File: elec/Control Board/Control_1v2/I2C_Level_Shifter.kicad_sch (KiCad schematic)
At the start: 21 parts, among them J201 0.100_2Pin, J202 Conn_01x04, Q201 BSS138, Q202 BSS138

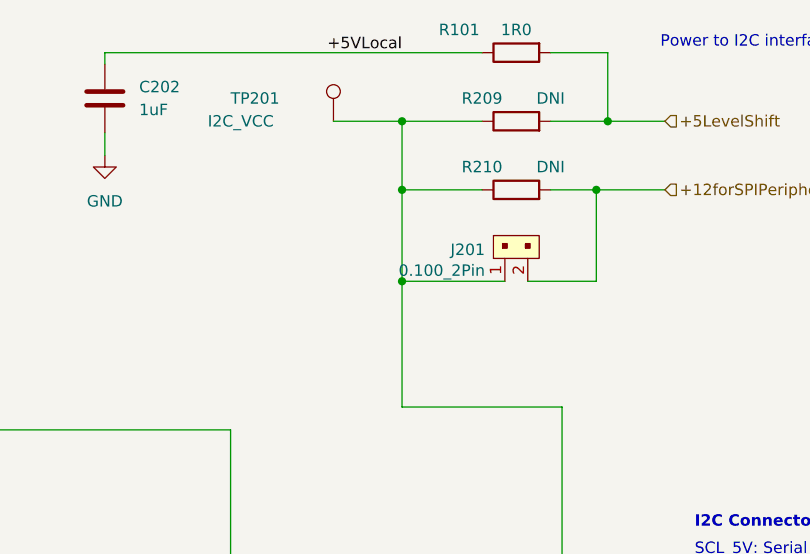
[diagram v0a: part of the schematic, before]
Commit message: PCB V1.2. Add test points of many colors.
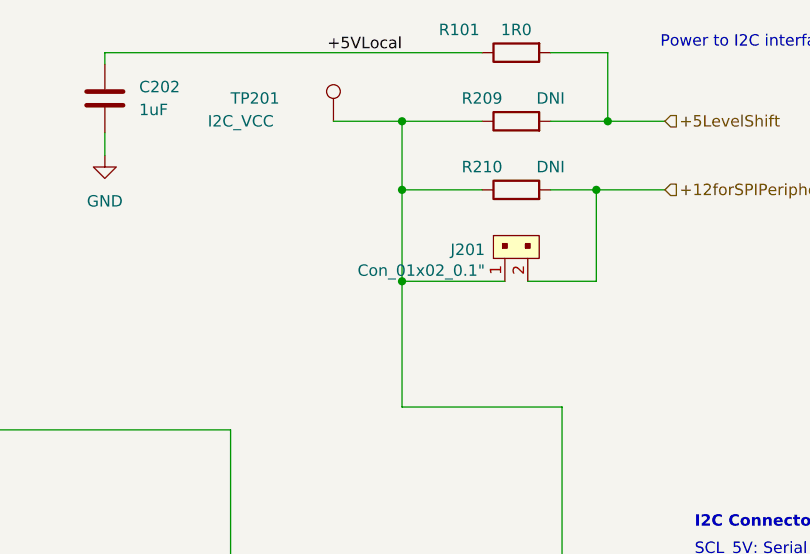
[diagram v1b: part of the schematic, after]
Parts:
- J201: value 0.100_2Pin -> Con_01x02_0.1"; Cost 0.1458 -> 0.0115; Distributor 1 PN C168673 -> C492401; MPN 68000-102HLF -> PZ254V-11-02P; Manufacturer Amphenol ICC -> XFCN
- TP201, TP202, TP203: Cost NA -> 0.0696; Distributor 1 NA -> JLCPCB; Distributor 1 PN NA -> C5277086; MPN (none) -> RH-5000; Manufacturer (none) -> ronghe
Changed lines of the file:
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@@
       (effects (font (size 1.27 1.27)) hide)
     )
-    (property "Distributor 1" "NA" (at 251.46 140.97 0)
-      (effects (font (size 1.27 1.27)) hide)
-    )
-    (property "Distributor 1 PN" "NA" (at 251.46 140.97 0)
-      (effects (font (size 1.27 1.27)) hide)
-    )
-    (property "Cost" "NA" (at 251.46 140.97 0)
+    (property "Distributor 1" "JLCPCB" (at 251.46 140.97 0)
+      (effects (font (size 1.27 1.27)) hide)
+    )
+    (property "Distributor 1 PN" "C5277086" (at 251.46 140.97 0)
+      (effects (font (size 1.27 1.27)) hide)
+    )
+    (property "Cost" "0.0696" (at 251.46 140.97 0)
       (effects (font (size 1.27 1.27)) hide)
     )
     (property "LongLead" "NO" (at 251.46 140.97 0)
+      (effects (font (size 1.27 1.27)) hide)
+    )
+    (property "Description" "Test Points/Test Rings ROHS red" (at 251.46 140.97 0)
+      (effects (font (size 1.27 1.27)) hide)
+    )
+    (property "MPN" "RH-5000 " (at 251.46 140.97 0)
+      (effects (font (size 1.27 1.27)) hide)
+    )
+    (property "Manufacturer" "ronghe " (at 251.46 140.97 0)
       (effects (font (size 1.27 1.27)) hide)
     )
@@
       (effects (font (size 1.27 1.27)) hide)
     )
-    (property "Distributor 1" "NA" (at 251.46 125.73 0)
-      (effects (font (size 1.27 1.27)) hide)
-    )
-    (property "Distributor 1 PN" "NA" (at 251.46 125.73 0)
-      (effects (font (size 1.27 1.27)) hide)
-    )
-    (property "Cost" "NA" (at 251.46 125.73 0)
+    (property "Distributor 1" "JLCPCB" (at 251.46 125.73 0)
+      (effects (font (size 1.27 1.27)) hide)
+    )
+    (property "Distributor 1 PN" "C5277086" (at 251.46 125.73 0)
+      (effects (font (size 1.27 1.27)) hide)
+    )
+    (property "Cost" "0.0696" (at 251.46 125.73 0)
       (effects (font (size 1.27 1.27)) hide)
     )
     (property "LongLead" "NO" (at 251.46 125.73 0)
+      (effects (font (size 1.27 1.27)) hide)
+    )
+    (property "Description" "Test Points/Test Rings ROHS red" (at 251.46 125.73 0)
+      (effects (font (size 1.27 1.27)) hide)
+    )
+    (property "MPN" "RH-5000 " (at 251.46 125.73 0)
+      (effects (font (size 1.27 1.27)) hide)
+    )
+    (property "Manufacturer" "ronghe " (at 251.46 125.73 0)
       (effects (font (size 1.27 1.27)) hide)
     )
@@
       (effects (font (size 1.27 1.27)) hide)
     )
-    (property "Distributor 1" "NA" (at 238.76 68.58 0)
-      (effects (font (size 1.27 1.27)) hide)
-    )
-    (property "Distributor 1 PN" "NA" (at 238.76 68.58 0)
-      (effects (font (size 1.27 1.27)) hide)
-    )
-    (property "Cost" "NA" (at 238.76 68.58 0)
+    (property "Distributor 1" "JLCPCB" (at 238.76 68.58 0)
+      (effects (font (size 1.27 1.27)) hide)
+    )
+    (property "Distributor 1 PN" "C5277086" (at 238.76 68.58 0)
+      (effects (font (size 1.27 1.27)) hide)
+    )
+    (property "Cost" "0.0696" (at 238.76 68.58 0)
       (effects (font (size 1.27 1.27)) hide)
     )
     (property "LongLead" "NO" (at 238.76 68.58 0)
+      (effects (font (size 1.27 1.27)) hide)
+    )
+    (property "Description" "Test Points/Test Rings ROHS red" (at 238.76 68.58 0)
+      (effects (font (size 1.27 1.27)) hide)
+    )
+    (property "MPN" "RH-5000 " (at 238.76 68.58 0)
+      (effects (font (size 1.27 1.27)) hide)
+    )
+    (property "Manufacturer" "ronghe " (at 238.76 68.58 0)
       (effects (font (size 1.27 1.27)) hide)
     )
@@
       (effects (font (size 1.27 1.27)) (justify right))
     )
-    (property "Value" "0.100_2Pin" (at 255.6002 85.1662 0)
+    (property "Value" "Con_01x02_0.1\"" (at 255.6002 85.1662 0)
       (effects (font (size 1.27 1.27)) (justify right))
     )
@@
       (effects (font (size 1.524 1.524)) (justify left) hide)
     )
-    (property "MPN" "68000-102HLF" (at 262.89 96.52 0)
+    (property "MPN" "PZ254V-11-02P" (at 262.89 96.52 0)
       (effects (font (size 1.524 1.524)) (justify left) hide)
     )
@@
       (effects (font (size 1.524 1.524)) (justify left) hide)
     )
-    (property "Description" "HEADER VERT 2POS 2.54MM" (at 262.89 109.22 0)
+    (property "Description" "Direct Insert Policy 2.5mm 2P 6mm -40℃~+105℃ 3mm 2.54mm Single Row Black Brass 1x2P Plugin,P=2.54mm Pin Headers ROHS" (at 262.89 109.22 0)
       (effects (font (size 1.524 1.524)) (justify left) hide)
     )
-    (property "Manufacturer" "Amphenol ICC" (at 262.89 111.76 0)
+    (property "Manufacturer" "XFCN" (at 262.89 111.76 0)
       (effects (font (size 0 0)) (justify left) hide)
     )
@@
       (effects (font (size 1.27 1.27)) hide)
     )
-    (property "Distributor 1 PN" "C168673" (at 257.81 83.82 0)
-      (effects (font (size 1.27 1.27)) hide)
-    )
-    (property "Cost" "0.1458" (at 257.81 83.82 0)
-      (effects (font (size 1.27 1.27)) hide)
-    )
+    (property "Distributor 1 PN" "C492401" (at 257.81 83.82 0)
+      (effects (font (size 1.27 1.27)) hide)
+    )
+    (property "Cost" "0.0115" (at 257.81 83.82 0)
+      (effects (font (size 1.27 1.27)) hide)
+    )

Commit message: PCB V1.2. Fixes to parts for BOM and PL.
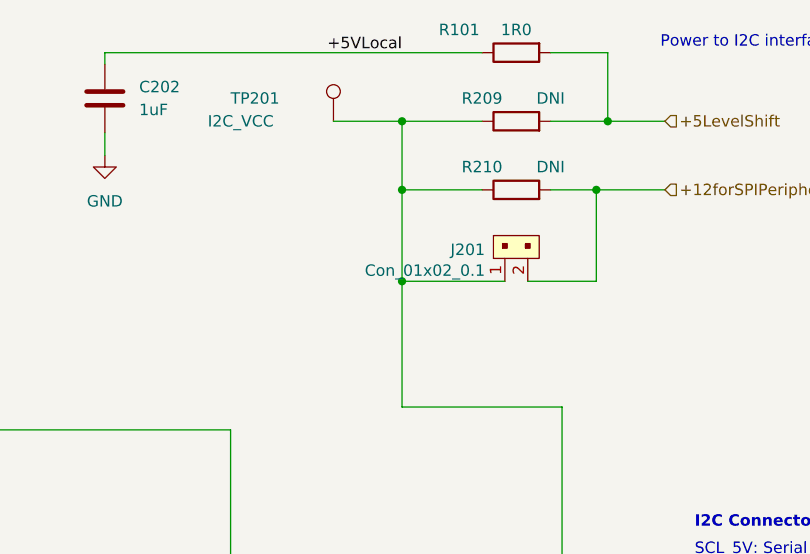
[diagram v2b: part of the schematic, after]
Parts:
- J201: value Con_01x02_0.1" -> Con_01x02_0.1
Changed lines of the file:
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@@
       (effects (font (size 1.27 1.27)) (justify right))
     )
-    (property "Value" "Con_01x02_0.1\"" (at 255.6002 85.1662 0)
+    (property "Value" "Con_01x02_0.1" (at 255.6002 85.1662 0)
       (effects (font (size 1.27 1.27)) (justify right))
     )
